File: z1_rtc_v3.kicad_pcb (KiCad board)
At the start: 2 copper layers, 62.5 x 51 mm, 63 parts, among them J1 Conn_01x05, J10 Conn_01x02, J2 61200621621, J3 Conn_01x11, J4 Conn_01x11, J5 Conn_01x11, J6 Conn_01x11, J7 691137710002, J8 USB_B_Micro, J9 Conn_01x02, U1 LCMXO2-1200HC-4SG32C, U2 ATmega328PB-AU, U3 FT230XS, Y1 Crystal_Small

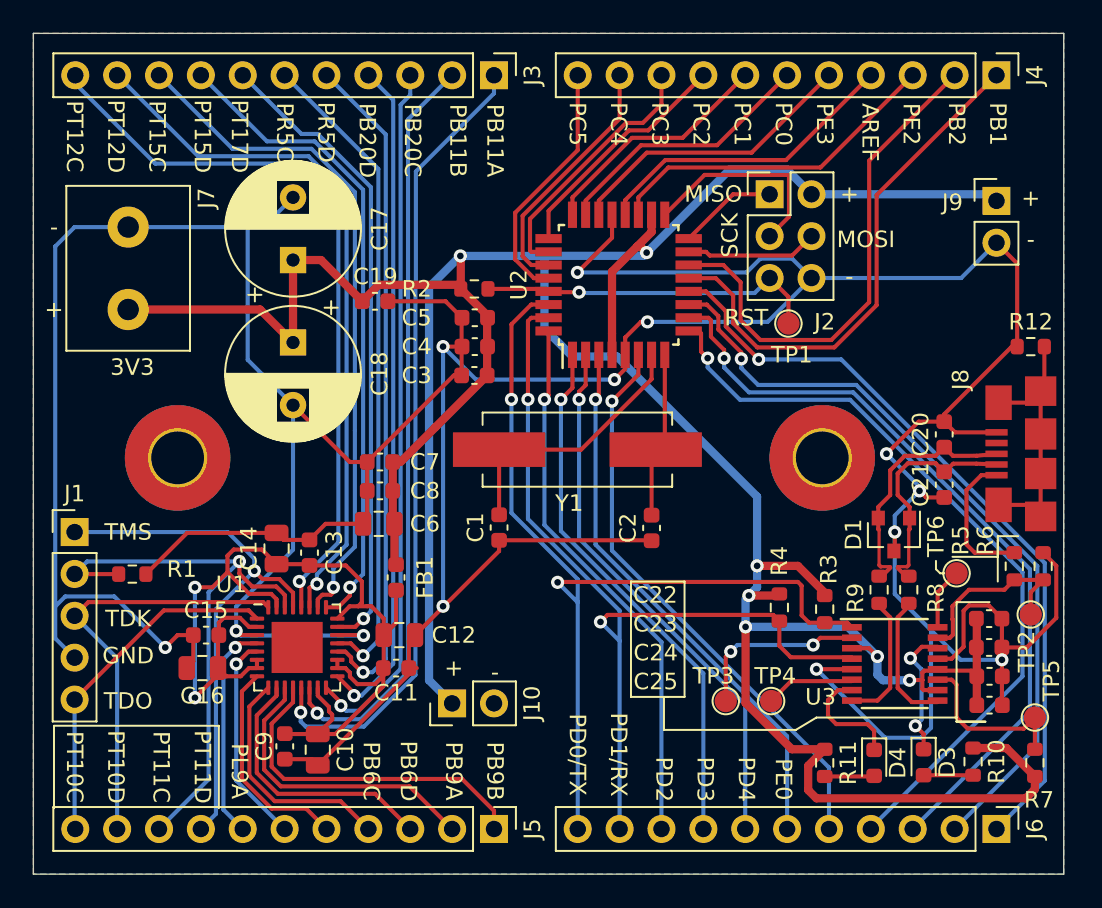
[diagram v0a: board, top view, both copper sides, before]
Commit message: finished routing v3.3
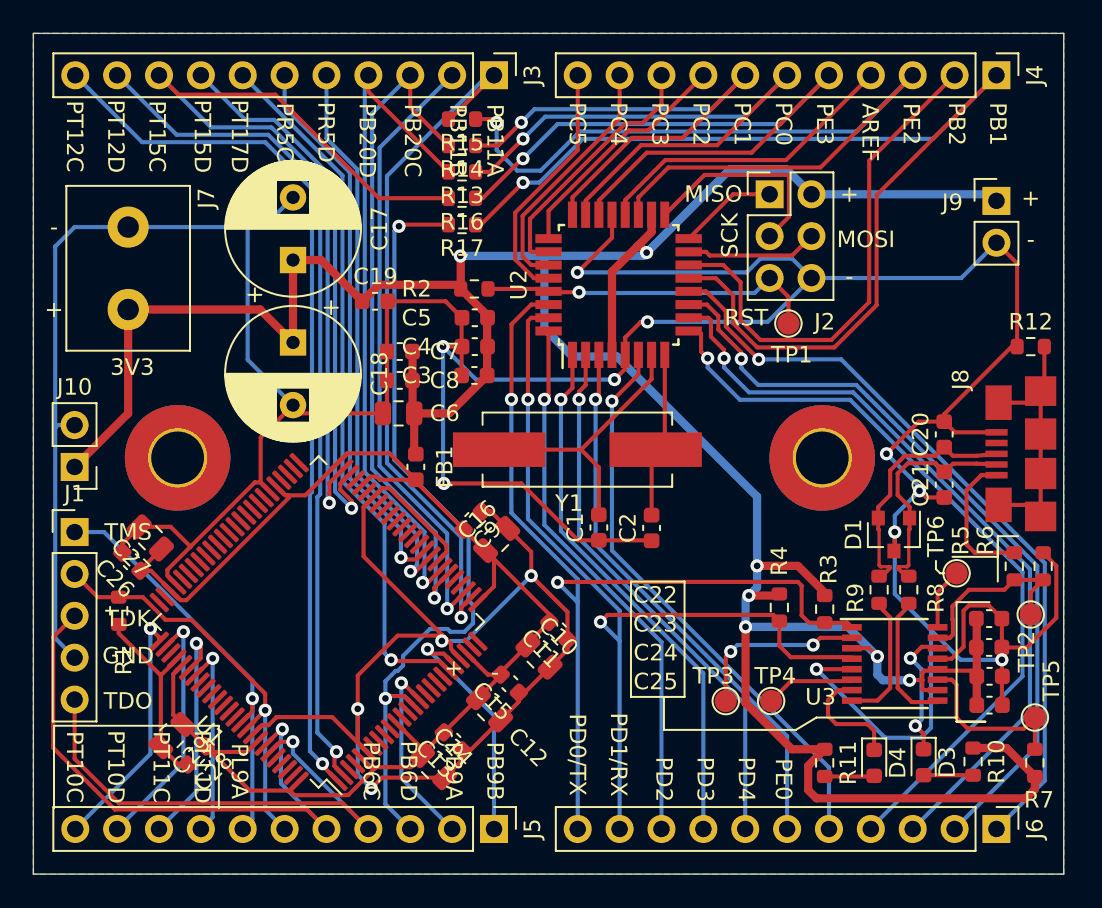
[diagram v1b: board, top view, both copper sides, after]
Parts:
- removed  : MountingHole_3.2mm_M3_Pad_TopBottom, MountingHole:MountingHole_3.2mm_M3_Pad_TopBottom (x2)
- added ?: MountingHole_3.2mm_M3_Pad_TopBottom, MountingHole:MountingHole_3.2mm_M3_Pad_TopBottom, F.Cu at (47.9, 25.8)
- added ?: MountingHole_3.2mm_M3_Pad_TopBottom, MountingHole:MountingHole_3.2mm_M3_Pad_TopBottom, F.Cu at (8.75, 25.8)
- added C26: 0.1uF, Capacitor_SMD:C_0603_1608Metric, F.Cu at (5.95, 32.0)
- added C27: 10nF, Capacitor_SMD:C_0805_2012Metric, F.Cu at (7.10, 30.6)
- added C28: 0.1uF, Capacitor_SMD:C_0603_1608Metric, F.Cu at (9.90, 43.8)
- added C29: 10nF, Capacitor_SMD:C_0805_2012Metric, F.Cu at (8.40, 42.6)
- added R13: 0R, Resistor_SMD:R_0603_1608Metric, F.Cu at (26.0, 8.40)
- added R14: 0R, Resistor_SMD:R_0603_1608Metric, F.Cu at (26.0, 6.80)
- added R15: 0R, Resistor_SMD:R_0603_1608Metric, F.Cu at (26.0, 5.20)
- added R16: 0R, Resistor_SMD:R_0603_1608Metric, F.Cu at (26.0, 10.0)
- added R17: 0R, Resistor_SMD:R_0603_1608Metric, F.Cu at (26.0, 11.6)
- U1: value LCMXO2-1200HC-4SG32C -> LCMXO2-2000HC-5TG100I; footprint Package_DFN_QFN:QFN-32-1EP_5x5mm_P0.5mm_EP3.1x3.1mm -> Package_QFP:TQFP-100_14x14mm_P0.5mm
- moved J10 27.0 mm to (2.50, 26.3), turned to 180 degrees
- moved C16 19.5 mm to (28.1, 30.7), turned to 45 degrees
- moved C15 18.7 mm to (28.9, 39.4), turned to 315 degrees
- moved C9 17.8 mm to (26.7, 29.5), turned to 45 degrees
- moved C14 16.3 mm to (24.3, 44.5), turned to 315 degrees
- moved C10 14.6 mm to (30.7, 37.8), turned to 315 degrees
- moved C13 14.4 mm to (25.4, 42.9), turned to 315 degrees
- moved C11 10.1 mm to (31.8, 36.2), turned to 315 degrees
- moved C12 7.07 mm to (27.7, 41.0), turned to 315 degrees
- moved C7 6.81 mm to (22.2, 19.3)
- moved C8 6.81 mm to (22.2, 21.1)
- moved C6 6.81 mm to (22.1, 23.1)
- moved FB1 6.81 mm to (23.2, 26.3)
- moved C1 6.05 mm to (34.3, 30.0)
- moved R1 2.37 mm to (5.17, 35.0), turned to 270 degrees
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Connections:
- J3 pad 1: PB11A -> PB5A
- J3 pad 10: PT12D -> PL2B
- J3 pad 11: PT12C -> PL2A
- J3 pad 2: PB11B -> PB5B
- J3 pad 3: PB20C -> PB8A
- J3 pad 4: PB20D -> PB8B
- J3 pad 5: PR5D -> PB11A
- J3 pad 6: PR5C -> PB11B
- J3 pad 7: PT17D -> PL12A
- J3 pad 8: PT15D -> PB25A
- J3 pad 9: PT15C -> PB25B
- J5 pad 1: PB9B -> PL12B
- J5 pad 10: TDI -> PT24C
- J5 pad 11: TDO -> PT24D
- J5 pad 2: PB9A -> PL9B
- J5 pad 3: PB6D -> PL9A
- J5 pad 4: PB6C -> TDO
- J5 pad 5: PB4C -> TDI
- J5 pad 6: PL9B -> TCK
- J5 pad 7: PL9A -> TMS
- J5 pad 8: TMS -> PT20C
- J5 pad 9: TCK -> PT20D
- U1 pad 1: TDO -> PL2A
- U1 pad 10: PB6D -> Net-(U1-Pad10)
- U1 pad 11: PB9A -> +3.3VP
- U1 pad 12: PB9B -> Net-(U1-Pad12)
- U1 pad 13: PB11A -> Net-(U1-Pad13)
- U1 pad 14: PB11B -> PL9A
- U1 pad 15: +3.3VP -> PL9B
- U1 pad 16: PB20C -> Net-(U1-Pad16)
- U1 pad 17: PB20D -> Net-(U1-Pad17)
- U1 pad 18: +3.3VP -> Net-(U1-Pad18)
- U1 pad 19: +3.3VP -> Net-(U1-Pad19)
- U1 pad 2: +3.3VP -> PL2B
- U1 pad 20: PR5D -> PL12A
- U1 pad 21: PR5C -> PL12B
- U1 pad 23: PT17D -> +3.3VP
- U1 pad 24: +3.3VP -> Net-(U1-Pad24)
- U1 pad 25: PT15D -> Net-(U1-Pad25)
- U1 pad 26: PT15C -> +3.3VP
- U1 pad 27: PT12D -> PB5A
- U1 pad 28: PT12C -> PB5B
- U1 pad 29: TMS -> Net-(U1-Pad29)
- U1 pad 3: GND -> Net-(U1-Pad3)
- U1 pad 30: TCK -> Net-(U1-Pad30)
- U1 pad 31: +3.3VP -> PB8A
- U1 pad 32: TDI -> PB8B
- U1 pad 33: (no net) -> GND
- U1 pad 4: PL9A -> Net-(U1-Pad4)
- U1 pad 5: PL9B -> +3.3VP
- U1 pad 6: +3.3VP -> GND
- U1 pad 7: +3.3VP -> Net-(U1-Pad7)
- U1 pad 8: PB4C -> Net-(U1-Pad8)
- U1 pad 9: PB6C -> Net-(U1-Pad9)
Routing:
- net PB25B: track 0.00 -> 55.5 mm, vias 0 -> 1
- net PL2A: track 0.00 -> 53.9 mm, vias 0 -> 1
- net PL2B: track 0.00 -> 51.7 mm, vias 0 -> 1
- net PT12C: track 45.1 -> 0.00 mm, vias 1 -> 0
- net PB5A: track 0.00 -> 43.1 mm, vias 0 -> 1
- net PT12D: track 43.0 -> 0.00 mm, vias 1 -> 0
- net PL12A: track 0.00 -> 42.9 mm, vias 0 -> 1
- net PB20C: track 42.5 -> 0.00 mm, vias 1 -> 0
- net PB8B: track 0.00 -> 41.9 mm, vias 0 -> 1
- net PB8A: track 0.00 -> 41.4 mm, vias 0 -> 1
- net PT15C: track 41.2 -> 0.00 mm, vias 1 -> 0
- net PB20D: track 41.1 -> 0.00 mm, vias 1 -> 0
- net PR5D: track 40.8 -> 0.00 mm, vias 1 -> 0
- net PR5C: track 39.8 -> 0.00 mm, vias 1 -> 0
- net PT15D: track 39.4 -> 0.00 mm, vias 1 -> 0
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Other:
- net class Default: clearance 0.2 -> 0.127
- rule trace_clearance: 0.2 -> 0.127
- rule trace_min: 0.2 -> 0.127

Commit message: finish silks
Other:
- board text added: "PB25A"
- board text added: "PB25B"
- board text added: "PB5A"
- board text added: "PB5B"
- board text added: "PB8A"
- board text added: "PB8B"
- board text added: "PL12A"
- board text added: "PL12B"
- board text added: "PL2A"
- board text added: "PL2B"
- board text added: "PT12C/TDO"
- board text added: "PT12D/TDI"
- board text added: "PT16C/TCK"
- board text added: "PT16D/TMS"
- board text added: "PT20C"
- board text added: "PT20D"
- board text added: "PT24C"
- board text added: "PT24D"
- board text added: "TCK"
- board text added: "z1_rtc v3.3"
- board text removed: "PB20C"
- board text removed: "PB20D"
- board text removed: "PB4C"
- board text removed: "PB6C"
- board text removed: "PB6D"
- board text removed: "PB9A"
- board text removed: "PB9B"
- board text removed: "PR5C"
- board text removed: "PR5D"
- board text removed: "PT10C"
- board text removed: "PT10C TDO"
- board text removed: "PT10D"
- board text removed: "PT10D/TDI"
- board text removed: "PT11C"
- board text removed: "PT11C/TCK"
- board text removed: "PT11D"
- board text removed: "PT11D/TMS"
- board text removed: "PT12C"
- board text removed: "PT12D"
- board text removed: "PT15C"
- board text removed: "PT15D"
- board text removed: "PT17D"
